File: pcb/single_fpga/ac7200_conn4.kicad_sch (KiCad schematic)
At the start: 1 part, among them U97 ALINX AC7200 (XC7A200T-2FBG48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

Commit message: Changed position.
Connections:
- net GND: now also U97.CON4_10 (GND), U97.CON4_15 (GND), U97.CON4_16 (GND), U97.CON4_21 (GND), U97.CON4_22 (GND), U97.CON4_27 (GND), U97.CON4_28 (GND), U97.CON4_33 (GND), U97.CON4_34 (GND), U97.CON4_39 (GND), U97.CON4_40 (GND), U97.CON4_49 (GND), U97.CON4_50 (GND), U97.CON4_59 (GND), U97.CON4_60 (GND), U97.CON4_69 (GND), U97.CON4_70 (GND), U97.CON4_9 (GND)
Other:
- moved on the sheet: U97D

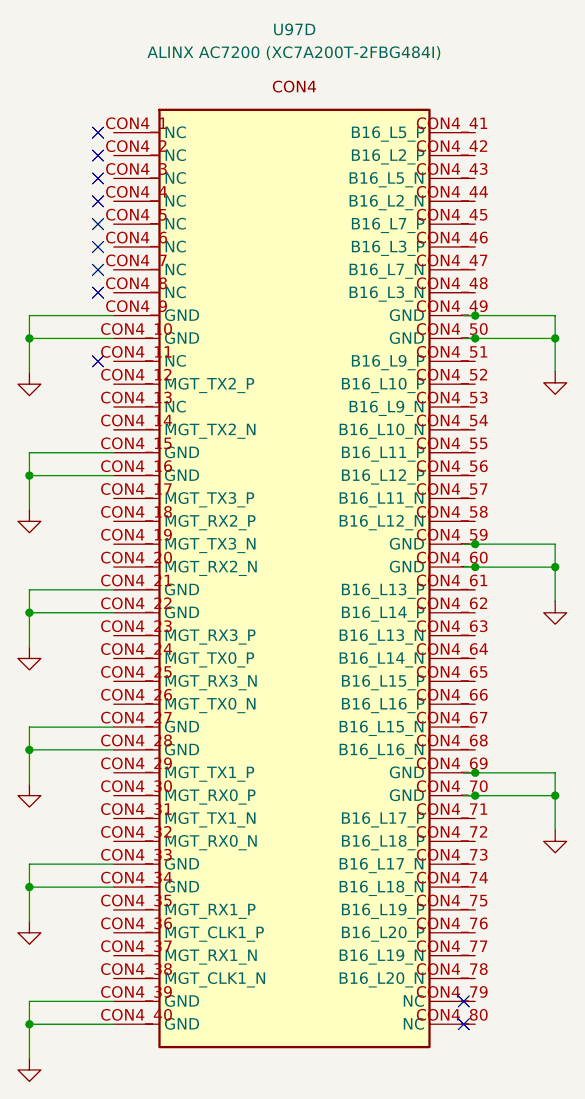
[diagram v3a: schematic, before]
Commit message: Reorganized sheets for two-boards. Fixed connector off-grid problems.
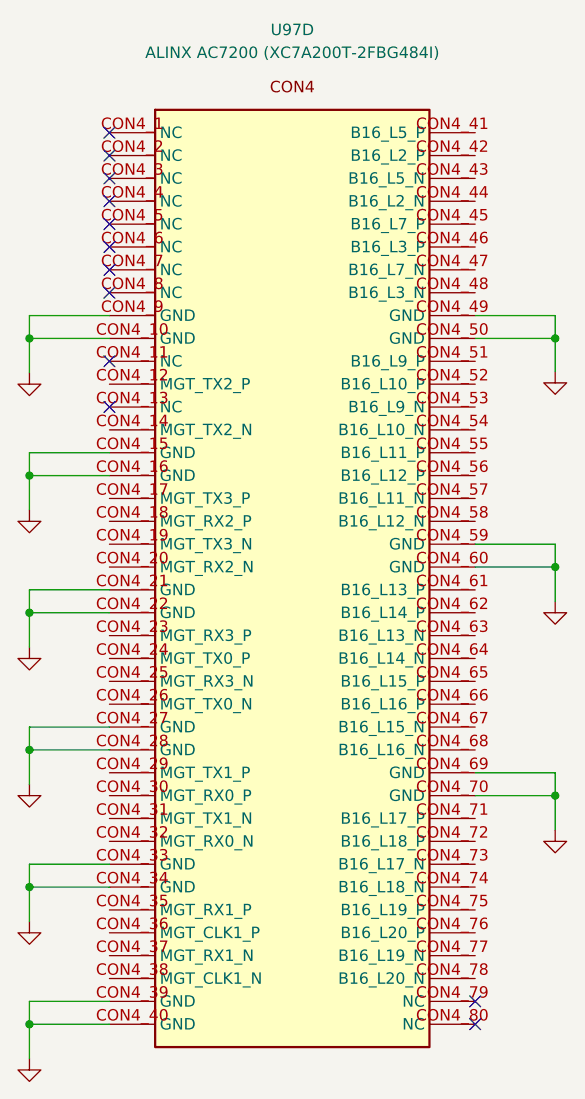
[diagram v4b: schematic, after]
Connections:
- no-connect marks 11 -> 12

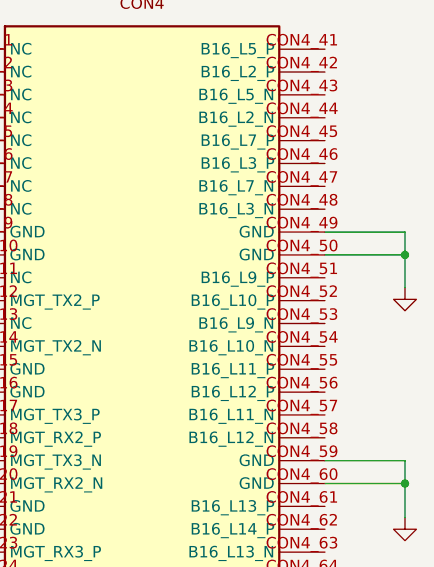
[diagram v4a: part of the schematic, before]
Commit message: Fixed another off-grid issue. Connected power and DATA_?? pins to inter-board connector.
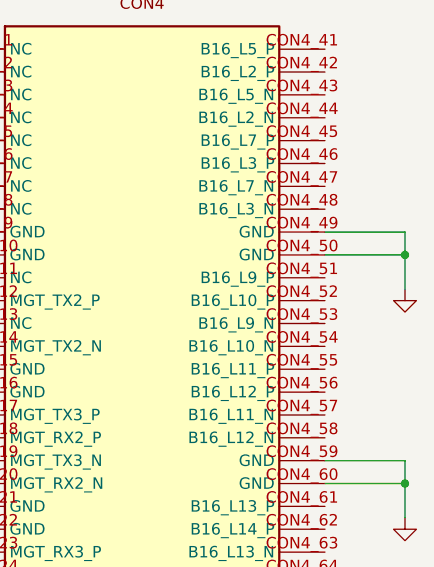
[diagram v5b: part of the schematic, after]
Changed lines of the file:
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@@
+	)
+	(junction
+		(at 147.32 127)
+		(diameter 0)
+		(color 0 0 0 0)
+	)
+	(junction
+		(at 88.9 91.44)
+		(diameter 0)
+		(color 0 0 0 0)
+	)
+	(junction
+		(at 88.9 121.92)
+		(diameter 0)
+		(color 0 0 0 0)
+	)
+	(junction
+		(at 88.9 106.68)
+		(diameter 0)
+		(color 0 0 0 0)
 	)
 	(junction
@@
 	)
 	(junction
-		(at 147.32 127)
-		(diameter 0)
-		(color 0 0 0 0)
-	)
-	(junction
-		(at 88.9 91.44)
-		(diameter 0)
-		(color 0 0 0 0)
-	)
-	(junction
-		(at 88.9 121.92)
-		(diameter 0)
-		(color 0 0 0 0)
-	)
-	(junction
-		(at 88.9 106.68)
-		(diameter 0)
-		(color 0 0 0 0)
-	)
-	(junction
 		(at 147.32 101.6)
 		(diameter 0)
@@
 	(wire
 		(pts
-			(xy 147.32 76.2) (xy 147.32 79.8663)
-		)
-		(stroke
-			(width 0)
-			(type default)
-		)
-	)
-	(wire
-		(pts
 			(xy 88.9 73.66) (xy 88.9 76.2)
 		)
@@
 		(pts
 			(xy 88.9 152.4) (xy 97.79 152.4)
+		)
+		(stroke
+			(width 0)
+			(type default)
+		)
+	)
+	(wire
+		(pts
+			(xy 147.32 76.2) (xy 147.32 80.01)
 		)
 		(stroke
@@
 	(symbol
 		(lib_id "power:GND")
-		(at 147.32 79.8663 0)
+		(at 147.32 80.01 0)
 		(unit 1)
 		(body_style 1)
@@
 		(fields_autoplaced yes)
 		(property "Reference" "#PWR029"
-			(at 147.32 86.2163 0)
+			(at 147.32 86.36 0)
 			(hide yes)
 			(show_name no)
@@
 		)
 		(property "Value" "GND"
-			(at 147.32 84.9463 0)
+			(at 147.32 85.09 0)
 			(hide yes)
 			(show_name no)
@@
 		)
 		(property "Footprint" ""
-			(at 147.32 79.8663 0)
+			(at 147.32 80.01 0)
 			(hide yes)
 			(show_name no)
@@
 		)
 		(property "Datasheet" ""
-			(at 147.32 79.8663 0)
+			(at 147.32 80.01 0)
 			(hide yes)
 			(show_name no)
@@
 		)
 		(property "Description" "Power symbol creates a global label with name \"GND\" , ground"
-			(at 147.32 79.8663 0)
-			(hide yes)
-			(show_name no)
+			(at 147.32 80.01 0)
+			(hide yes)
+			(show_name no)

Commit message: Updated all refdes's.
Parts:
- renumbered U97 to U109
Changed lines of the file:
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@@
 		(dnp no)
 		(fields_autoplaced yes)
-		(property "Reference" "#PWR023"
+		(property "Reference" "#PWR0459"
 			(at 147.32 111.76 0)
 			(hide yes)
@@
 			(project "top"
 				(path "/12638caa-1907-413e-8e98-06abbbf6ccbc/8ee3463b-0816-4e24-be6c-9811f4c49ad3/e6837c47-bc22-43f8-ac12-31efd060f9ae"
-					(reference "#PWR023")
+					(reference "#PWR0459")
 					(unit 1)
 				)
@@
 		(dnp no)
 		(fields_autoplaced yes)
-		(property "Reference" "#PWR024"
+		(property "Reference" "#PWR0456"
 			(at 88.9 147.32 0)
 			(hide yes)
@@
 			(project "top"
 				(path "/12638caa-1907-413e-8e98-06abbbf6ccbc/8ee3463b-0816-4e24-be6c-9811f4c49ad3/e6837c47-bc22-43f8-ac12-31efd060f9ae"
-					(reference "#PWR024")
+					(reference "#PWR0456")
 					(unit 1)
 				)
@@
 		(dnp no)
 		(fields_autoplaced yes)
-		(property "Reference" "#PWR025"
+		(property "Reference" "#PWR0460"
 			(at 147.32 137.16 0)
 			(hide yes)
@@
 			(project "top"
 				(path "/12638caa-1907-413e-8e98-06abbbf6ccbc/8ee3463b-0816-4e24-be6c-9811f4c49ad3/e6837c47-bc22-43f8-ac12-31efd060f9ae"
-					(reference "#PWR025")
+					(reference "#PWR0460")
 					(unit 1)
 				)
@@
 		(dnp no)
 		(fields_autoplaced yes)
-		(property "Reference" "#PWR026"
+		(property "Reference" "#PWR0455"
 			(at 88.9 132.08 0)
 			(hide yes)
@@
 			(project "top"
 				(path "/12638caa-1907-413e-8e98-06abbbf6ccbc/8ee3463b-0816-4e24-be6c-9811f4c49ad3/e6837c47-bc22-43f8-ac12-31efd060f9ae"
-					(reference "#PWR026")
+					(reference "#PWR0455")
 					(unit 1)
 				)
@@
 		(dnp no)
 		(fields_autoplaced yes)
-		(property "Reference" "#PWR027"
+		(property "Reference" "#PWR0453"
 			(at 88.9 101.6 0)
 			(hide yes)
@@
 			(project "top"
 				(path "/12638caa-1907-413e-8e98-06abbbf6ccbc/8ee3463b-0816-4e24-be6c-9811f4c49ad3/e6837c47-bc22-43f8-ac12-31efd060f9ae"
-					(reference "#PWR027")
+					(reference "#PWR0453")
 					(unit 1)
 				)
@@
 		(dnp no)
 		(fields_autoplaced yes)
-		(property "Reference" "#PWR028"
+		(property "Reference" "#PWR0454"
 			(at 88.9 116.84 0)
 			(hide yes)
@@
 			(project "top"
 				(path "/12638caa-1907-413e-8e98-06abbbf6ccbc/8ee3463b-0816-4e24-be6c-9811f4c49ad3/e6837c47-bc22-43f8-ac12-31efd060f9ae"
-					(reference "#PWR028")
+					(reference "#PWR0454")
 					(unit 1)
 				)
@@
 		(dnp no)
 		(fields_autoplaced yes)
-		(property "Reference" "#PWR029"
+		(property "Reference" "#PWR0458"
 			(at 147.32 86.36 0)
 			(hide yes)
@@
 			(project "top"
 				(path "/12638caa-1907-413e-8e98-06abbbf6ccbc/8ee3463b-0816-4e24-be6c-9811f4c49ad3/e6837c47-bc22-43f8-ac12-31efd060f9ae"
-					(reference "#PWR029")
+					(reference "#PWR0458")
 					(unit 1)
 				)
@@
 		(dnp no)
 		(fields_autoplaced yes)
-		(property "Reference" "U97"
+		(property "Reference" "U109"
 			(at 118.11 41.91 0)
 			(show_name no)
@@
 			(project "top"
 				(path "/12638caa-1907-413e-8e98-06abbbf6ccbc/8ee3463b-0816-4e24-be6c-9811f4c49ad3/e6837c47-bc22-43f8-ac12-31efd060f9ae"
-					(reference "U97")
+					(reference "U109")
 					(unit 4)
 				)
@@
 		(dnp no)
 		(fields_autoplaced yes)
-		(property "Reference" "#PWR030"
+		(property "Reference" "#PWR0457"
 			(at 88.9 162.56 0)
 			(hide yes)
@@
 			(project "top"
 				(path "/12638caa-1907-413e-8e98-06abbbf6ccbc/8ee3463b-0816-4e24-be6c-9811f4c49ad3/e6837c47-bc22-43f8-ac12-31efd060f9ae"
-					(reference "#PWR030")
+					(reference "#PWR0457")
 					(unit 1)
 				)
@@
 		(dnp no)
 		(fields_autoplaced yes)
-		(property "Reference" "#PWR031"
+		(property "Reference" "#PWR0452"
 			(at 88.9 86.36 0)
 			(hide yes)
@@
 			(project "top"
 				(path "/12638caa-1907-413e-8e98-06abbbf6ccbc/8ee3463b-0816-4e24-be6c-9811f4c49ad3/e6837c47-bc22-43f8-ac12-31efd060f9ae"
-					(reference "#PWR031")
+					(reference "#PWR0452")
 					(unit 1)
 				)
